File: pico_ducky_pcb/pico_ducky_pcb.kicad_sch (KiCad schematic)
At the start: 20 parts

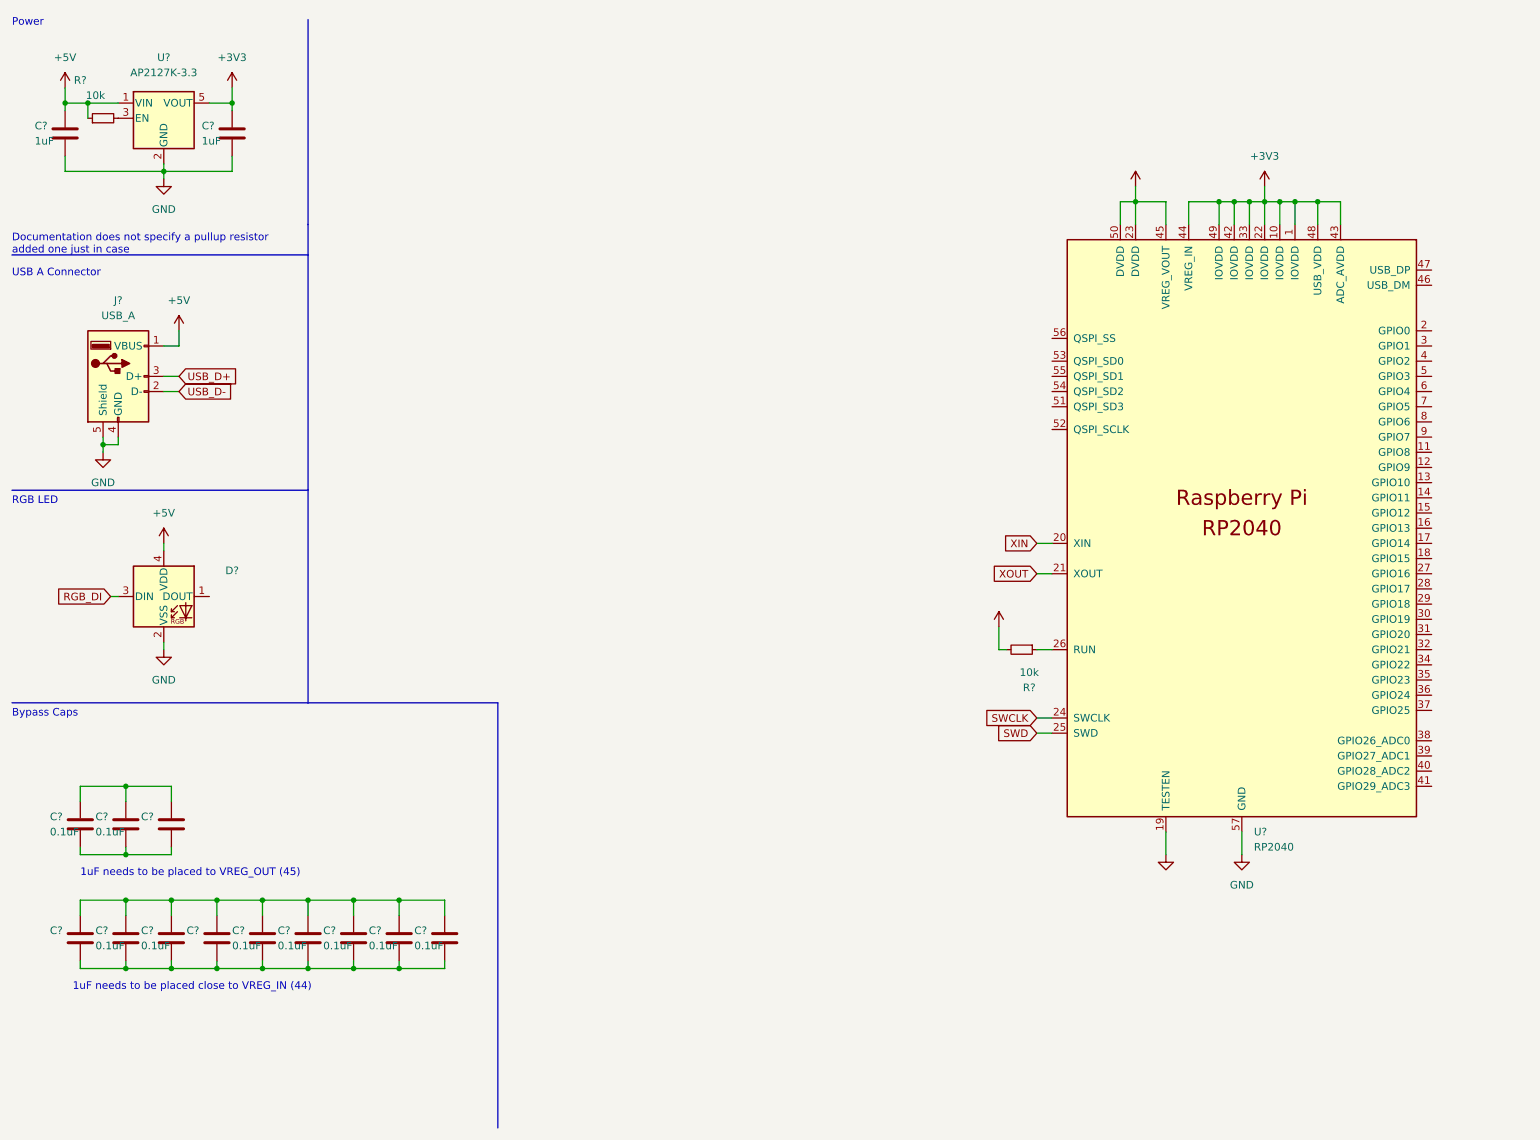
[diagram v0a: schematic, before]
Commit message: get the placement 90% switch out SW1 and SW2 to buttons that are 1mm thick
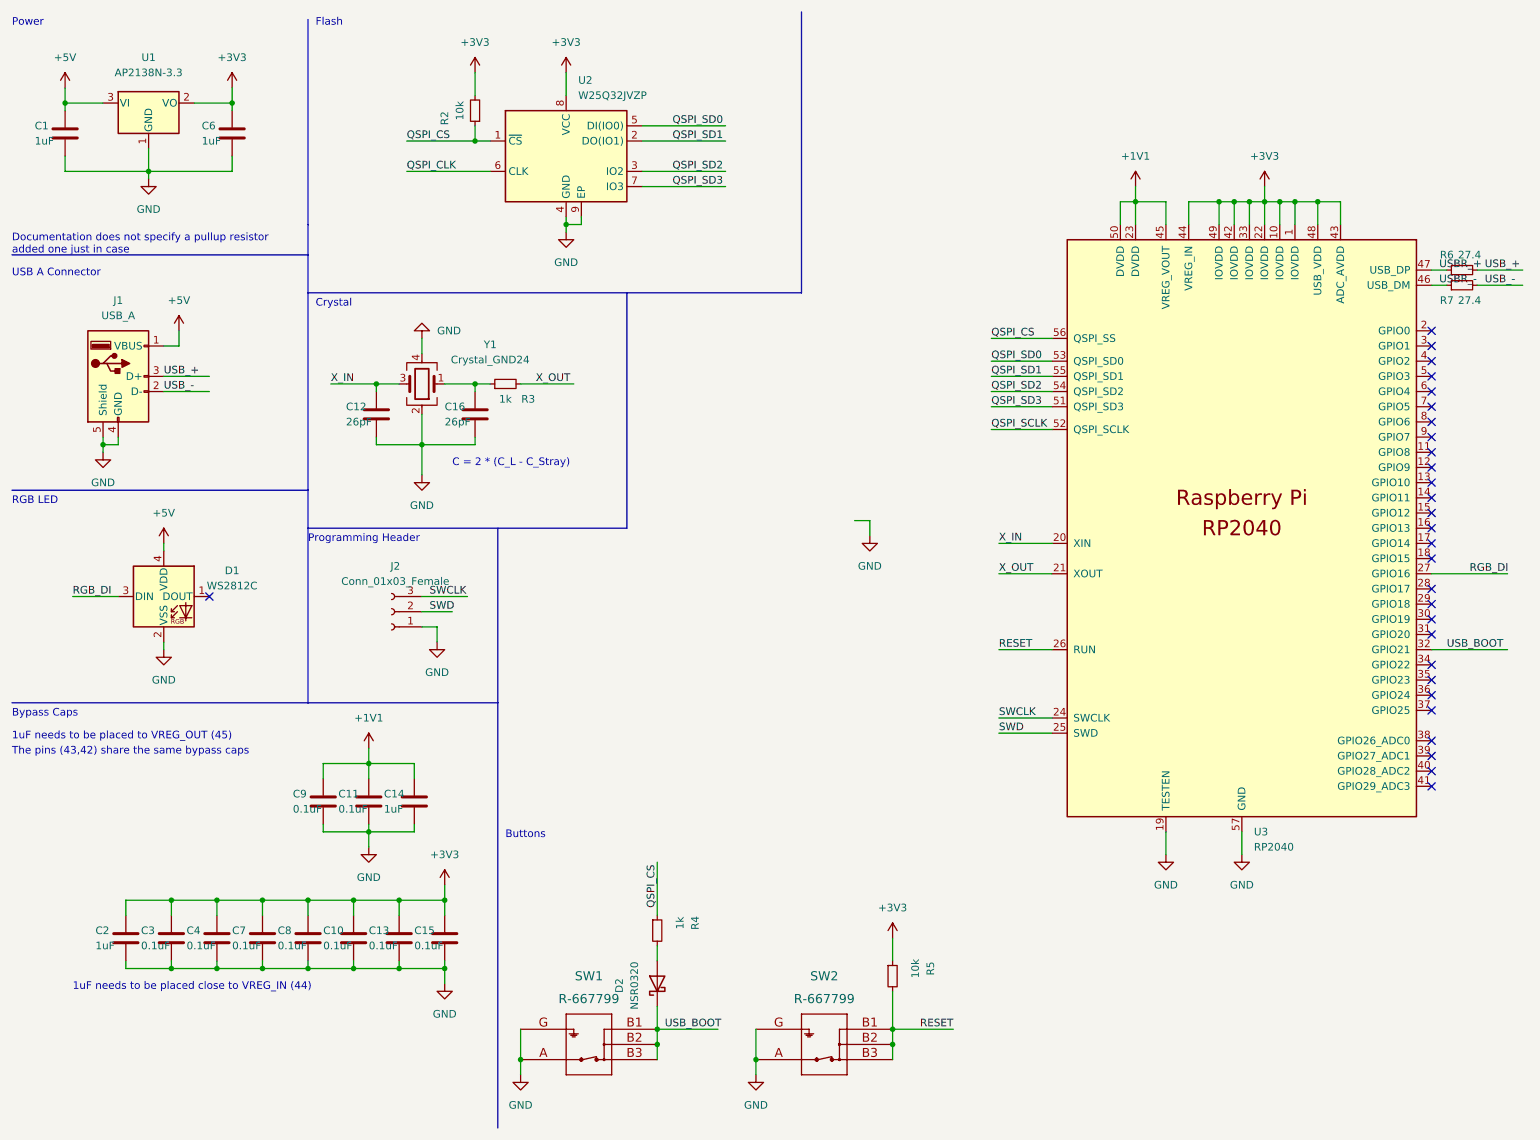
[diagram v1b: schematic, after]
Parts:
- removed C?: (no value), Capacitor_SMD:C_0402_1005Metric, symbol Device:C
- removed R?: 10k, Resistor_SMD:R_0402_1005Metric, symbol Device:R_Small
- removed U?: AP2127K-3.3, Package_TO_SOT_SMD:SOT-23-5, symbol Regulator_Linear:AP2127K-3.3
- added C12, C16: 26pF, Capacitor_SMD:C_0402_1005Metric, symbol Device:C
- added D2: NSR0320, Diode_SMD:D_SOD-323, symbol Diode:NSR0320
- added J2: Conn_01x03_Female, Connector_PinHeader_1.27mm:PinHeader_1x03_P1.27mm_Vertical, symbol Connector:Conn_01x03_Female
- added R2: 10k, Resistor_SMD:R_0402_1005Metric, symbol Device:R_Small
- added R3, R4: 1k, Resistor_SMD:R_0402_1005Metric, symbol Device:R_Small
- added R6, R7: 27.4, Resistor_SMD:R_0201_0603Metric, symbol Device:R_Small
- added SW1, SW2: R-667799, symbol 2022-04-30_19-21-11:R-667799
- added U1: AP2138N-3.3, Package_TO_SOT_SMD:SOT-23, symbol Regulator_Linear:AP2138N-3.3
- added U2: W25Q32JVZP, 8-UFDFN:W25Q80DVUXIE TR, symbol Memory_Flash:W25Q32JVZP
- added Y1: Crystal_GND24, Crystal:Crystal_SMD_2520-4Pin_2.5x2.0mm, symbol Device:Crystal_GND24
- C14, C2: renamed from C?; value (none) -> 1uF
- D1: renamed from D?; value (none) -> WS2812C; footprint (none) -> WS2812C:WS2812C-2020
- gave numbers to parts that had none: 14
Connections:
- net +1V1: now also C11.2, C14.2, C9.2
- net +3V3: now also C10.2, C13.2, C15.2, C2.2, C3.2, C4.2, C7.2, C8.2, R5.1, R2.2, U1.2 (VO), U2.8 (VCC); no longer R5.2
- net +5V: now also U1.3 (VI)
- net GND: now also C10.1, C11.1, C13.1, C14.1, C15.1, C2.1, C3.1, C4.1, C7.1, C8.1, C9.1, C12.1, C16.1, J2.1 (Pin_1), SW1.A, SW1.G, SW2.A, SW2.G, U1.1 (GND), U2.4 (GND), U2.9 (EP), Y1.2, Y1.4
- net RGB_DI: now also U3.27 (GPIO16)
- net SWCLK: now also J2.3 (Pin_3)
- net SWD: now also J2.2 (Pin_2)
- net RESET: now reaches U3.26 (RUN)
- net RESET: now also R5.2, SW2.B1, SW2.B2, SW2.B3; no longer R5.1
- net USB_BOOT: now reaches U3.32 (GPIO21)
- net USB_BOOT: now also D2.1 (K), SW1.B1, SW1.B2, SW1.B3
- net USBR_-: now reaches U3.46 (USB_DM)
- net USBR_-: now also R7.1
- net USBR_+: now reaches U3.47 (USB_DP)
- net USBR_+: now also R6.1
- net QSPI_SD3: now reaches U3.51 (QSPI_SD3)
- net QSPI_SD3: now also U2.7 (IO3)
- net QSPI_SCLK: now reaches U3.52 (QSPI_SCLK)
- net QSPI_SD0: now reaches U3.53 (QSPI_SD0)
- net QSPI_SD0: now also U2.5 (DI(IO0))
- net QSPI_SD2: now reaches U3.54 (QSPI_SD2)
- net QSPI_SD2: now also U2.3 (IO2)
- net QSPI_SD1: now reaches U3.55 (QSPI_SD1)
- net QSPI_SD1: now also U2.2 (DO(IO1))
- net QSPI_CS: now reaches U3.56 (QSPI_SS)
- net QSPI_CS: now also R2.1, R4.1, U2.1 (~{CS})
- net USB_D+ renamed USB_+
- net USB_+: now also R6.2
- net USB_D- renamed USB_-
- net USB_-: now also R7.2
- net XIN renamed X_IN
- net X_IN: now also C12.2, Y1.3
- net XOUT renamed X_OUT
- net X_OUT: now also R3.2
- new net: C16.2, R3.1, Y1.1
- new net: D2.2 (A), R4.2
- new net QSPI_CLK: U2.6 (CLK)
- no-connect marks 0 -> 29
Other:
- note added: "Buttons"
- note added: "C = 2 * (C_L - C_Stray)"
- note added: "Crystal"
- note added: "Flash"
- note added: "Programming Header"
- note added: "The pins (43,42) share the same bypass caps"
- moved on the sheet: C11, C14, C2, C3, C4, C9, R5

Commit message: finish most of the inpours, routing and vias
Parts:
- SW1, SW2: footprint (none) -> R-WHATEVER:R-667799
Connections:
- net QSPI_CLK is gone; now on net QSPI_SCLK: U2.6 (CLK)
- net +3V3: now also D1.4 (VDD)
- net +5V: no longer D1.4 (VDD)
- net RGB_DI: now also U3.15 (GPIO12); no longer U3.27 (GPIO16)
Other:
- moved on the sheet: D2, R4, R5, SW1, SW2

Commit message: pass erc
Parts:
- removed D1: WS2812C, WS2812C:WS2812C-2020, symbol LED:WS2812C
- removed U1: AP2138N-3.3, Package_TO_SOT_SMD:SOT-23, symbol Regulator_Linear:AP2138N-3.3
- added C5: 0.1uF, Capacitor_SMD:C_0201_0603Metric, symbol Device:C
- added D1: SK6812, LED_SMD:LED_SK6812_EC15_1.5x1.5mm, symbol LED:SK6812
- added U1: AP2127K-3.3, Package_TO_SOT_SMD:SOT-23-5, symbol Regulator_Linear:AP2127K-3.3
- C10, C11, C13, C15, C3, C4, C7, C8, C9: footprint Capacitor_SMD:C_0402_1005Metric -> Capacitor_SMD:C_0201_0603Metric
- R6, R7: footprint Resistor_SMD:R_0201_0603Metric -> Resistor_SMD:R_0402_1005Metric
- SW1: footprint R-WHATEVER:R-667799 -> (none)
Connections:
- net +3V3: now also C5.2, D1.3 (VDD), U1.5 (VOUT)
- net +5V: now also U1.1 (VIN), U1.3 (EN)
- net GND: now also C5.1, D1.1 (VSS), U1.2 (GND)
- net RGB_DI: now also D1.2 (DIN)

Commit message: finish the layout
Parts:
- SW1: footprint (none) -> R-WHATEVER:R-667799
- renumbered C2 to C14, C14 to C2
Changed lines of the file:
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@@
       (effects (font (size 1.524 1.524)))
     )
-    (property "Footprint" "" (id 2) (at 110.49 179.324 0)
+    (property "Footprint" "R-WHATEVER:R-667799" (id 2) (at 110.49 179.324 0)
       (effects (font (size 1.524 1.524)) hide)
     )
@@
   (symbol (lib_id "Device:C") (at 31.75 166.37 180) (unit 1)
     (in_bom yes) (on_board yes)
-    (property "Reference" "C2" (id 0) (at 26.67 165.1 0)
+    (property "Reference" "C14" (id 0) (at 26.67 165.1 0)
       (effects (font (size 1.27 1.27)) (justify right))
     )
@@
   (symbol (lib_id "Device:C") (at 80.01 143.51 180) (unit 1)
     (in_bom yes) (on_board yes)
-    (property "Reference" "C14" (id 0) (at 74.93 142.24 0)
+    (property "Reference" "C2" (id 0) (at 74.93 142.24 0)
       (effects (font (size 1.27 1.27)) (justify right))
     )
@@
       (reference "C1") (unit 1) (value "1uF") (footprint "Capacitor_SMD:C_0402_1005Metric")
     )
-    (path "/64d338e2-810f-40dd-b6e7-61458eef9140"
+    (path "/b5f66f1a-65bc-454c-a7b0-ea71256c3265"
       (reference "C2") (unit 1) (value "1uF") (footprint "Capacitor_SMD:C_0402_1005Metric")
     )
@@
       (reference "C13") (unit 1) (value "0.1uF") (footprint "Capacitor_SMD:C_0201_0603Metric")
     )
-    (path "/b5f66f1a-65bc-454c-a7b0-ea71256c3265"
+    (path "/64d338e2-810f-40dd-b6e7-61458eef9140"
       (reference "C14") (unit 1) (value "1uF") (footprint "Capacitor_SMD:C_0402_1005Metric")
     )
